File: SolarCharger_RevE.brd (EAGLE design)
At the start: 85 x 78 mm, 134 parts, among them CON1 CON_4X200MIL, CON2 USB_BMULTICOMP, CON3 ICSP, CON4 CON_3X100MIL, CON5 CON_3X100MIL, CON6 CON_8X200MIL, CON7 CON_2X100MIL, CON8 CON_3X100MIL, CON9 CON_6X3X2, IC1 MCP3428, IC10 AT45DB161E, IC11 TPS54428, IC12 MCP14A0153, IC13 MCP14A0153, IC2 INA213, IC3 MIC4605-1YM, IC4 INA213, IC5 PIC18F46J50, IC6 TS6001, IC7 LMT86, IC8 24AA16, IC9 TPS62120, Q1 NX3008NBKW, Q10 NTR4101PT1G, Q11 N-FET, Q12 N-FET, Q13 N-FET, Q14 N-FET, Q15 NX3008NBKW, Q2 PSMN6R0-30YL, Q3 NX3008NBKW, Q4 NTR4101PT1G, Q5 PSMN6R0-30YL, Q6 PSMN6R0-30YL, Q7 NX3008NBKW, Q8 NX3008NBKW, Q9 NX3008NBKW, X1 ABS07-120-32.768KHZ-T, X2 ABM3-8.000MHZ-D2Y-T, X3 USB_A, X4 USB_A

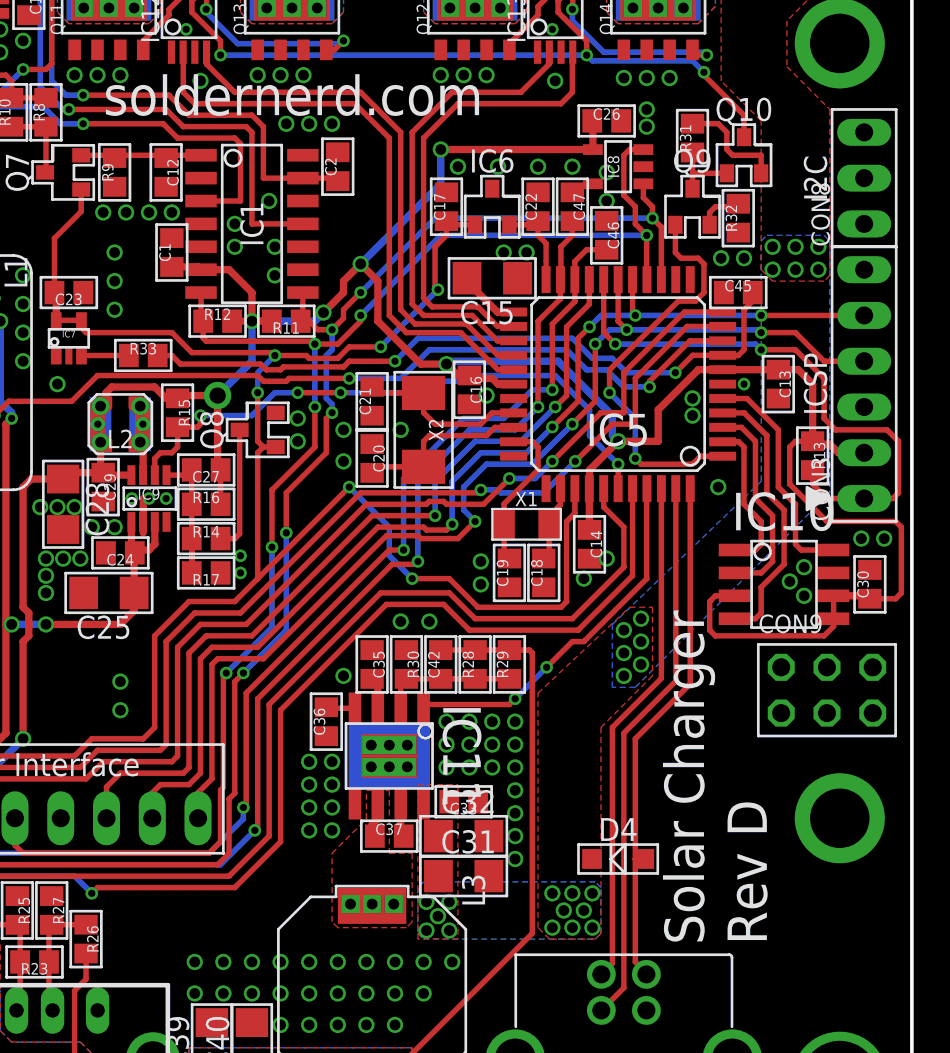
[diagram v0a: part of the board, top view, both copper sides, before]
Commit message: Revision E completed. Now with SPI and I2C headers
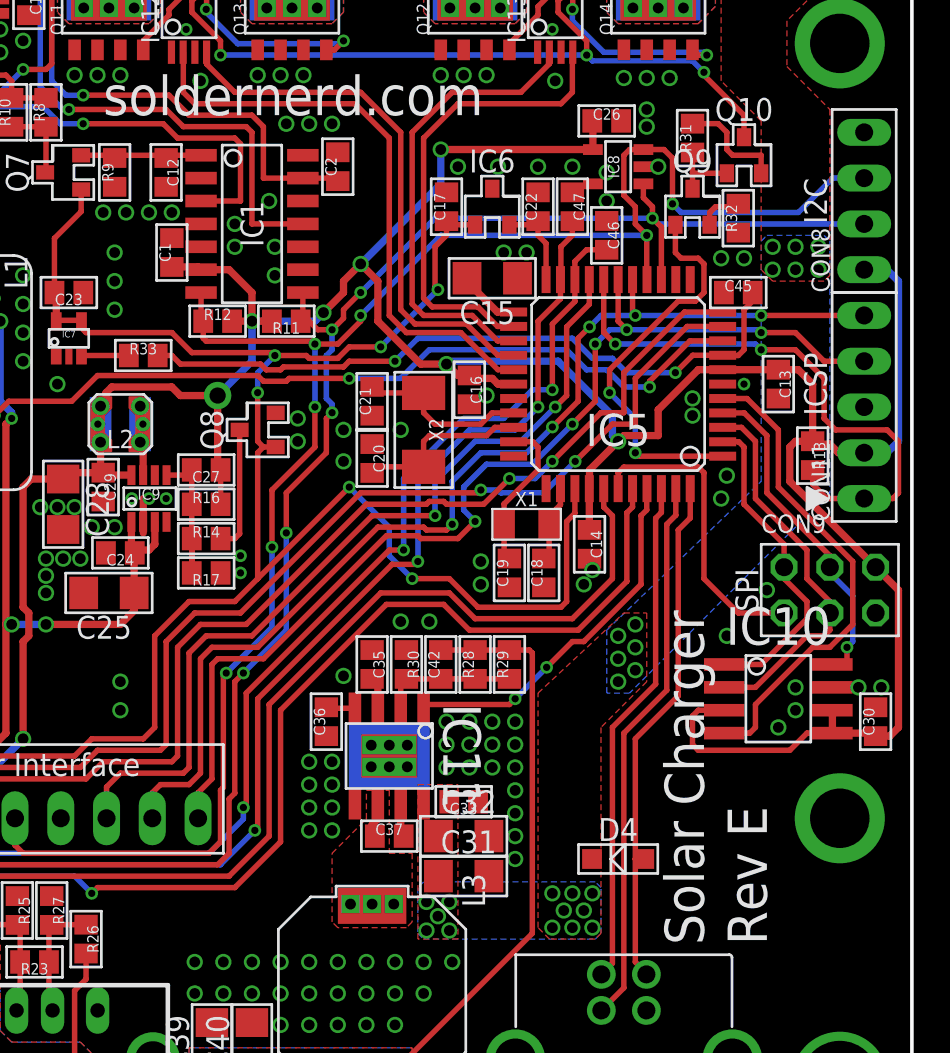
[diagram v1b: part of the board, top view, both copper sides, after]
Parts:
- removed CON3: ICSP, 00Connector:100MIL_6X
- removed R15: 100k, 00Resistor:R0805
- added CON11: CON_5X100MIL, 00Connector:100MIL_5X
- CON8: value CON_3X100MIL -> I2C; device 00Connector:100MIL_3X -> 00Connector:100MIL_4X
- CON9: value CON_6X3X2 -> SPI
- IC10: value AT45DB161E -> AT45DB321E; device 00Logic:SOIC8 -> 00Logic:EIAJ_SOIC8
- moved C30 7.63 mm to (90.5, 22.9)
- moved IC10 6.36 mm to (85.1, 24.1)
- moved CON9 5.56 mm to (87.9, 30.2)
- moved CON8 1.27 mm to (89.9, 51.8)
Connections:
- removed net PWR_GOOD: IC5.39, IC9.6, R15.2
- net !MCLR!: now also CON11.1; no longer CON3.1
- net !SS1!: now also IC5.5; no longer IC5.4
- net !SS2!: now also IC5.39
- net GND: now also CON11.3, CON8.4; no longer CON3.3, CON8.3
- net MISO: now also IC5.4; no longer IC5.5
- net MOSI: now also CON9.1; no longer CON9.3
- net PGC/ENC_A: now also CON11.5; no longer CON3.5
- net PGD/ENC_B: now also CON11.4; no longer CON3.4
- net SCLK: now also CON9.5; no longer CON9.1
- net SDA: now also CON8.3; no longer CON8.1
- net VCC: now also CON11.2, CON8.1, CON9.3; no longer CON3.2, CON9.5, R15.1
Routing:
- net PWR_GOOD: track 34.0 -> 0.00 mm, vias 4 -> 0
- net VCC: track 164.7 -> 183.8 mm
- net !SS2!: track 0.00 -> 17.0 mm
- net SDA: track 81.8 -> 97.8 mm, vias 6 -> 7
- net SCL: track 78.7 -> 90.5 mm
- net !SS1!: track 15.4 -> 26.7 mm
- net SCLK: track 11.6 -> 21.5 mm
- net MOSI: track 8.71 -> 17.9 mm
- net MISO: track 12.8 -> 18.6 mm, vias 0 -> 1
- net OUT_ON: track 22.7 -> 22.1 mm
- net !DISP_EN!: track 61.6 -> 61.0 mm
- net GND: vias 216 -> 220
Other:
- board text added: "A"
- board text added: "B"
- board text added: "January 2018 - Rev E"
- board text added: "MISO"
- board text added: "MOSI"
- board text added: "PB"
- board text added: "PGC"
- board text added: "PGD"
- board text added: "Rev E"
- board text added: "SCL"
- board text added: "SCLK"
- board text added: "SDA"
- board text added: "SPI"
- board text added: "VCC"
- board text added: "~EN"
- board text added: "~MC"
- board text added: "~SS2"
- board text removed: "Rev D"
- board text removed: "September 2017 - Rev D"

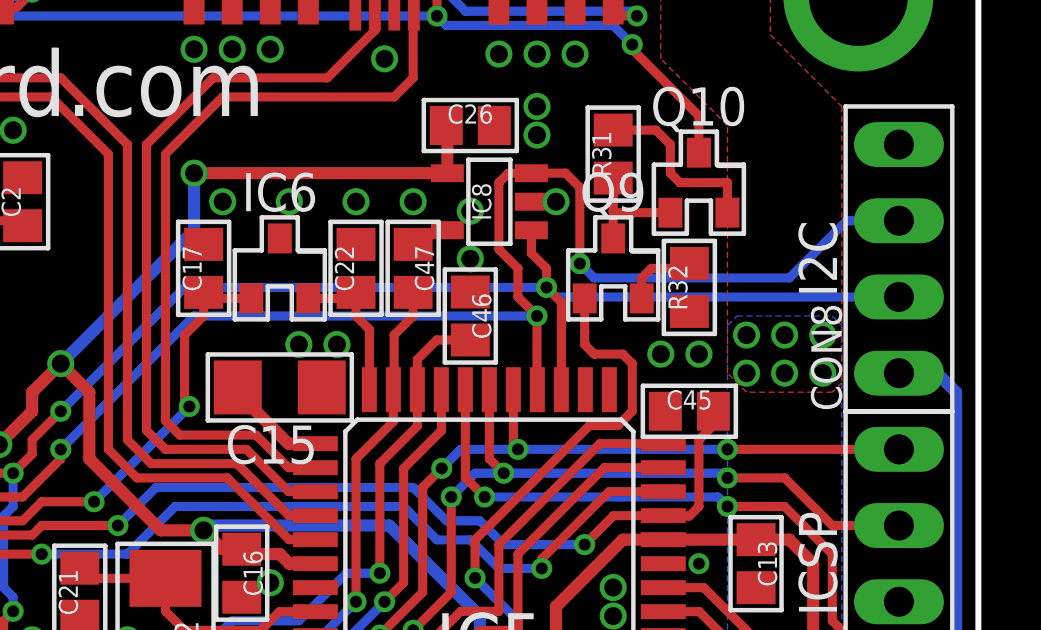
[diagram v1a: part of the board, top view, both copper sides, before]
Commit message: Some ground connections improved
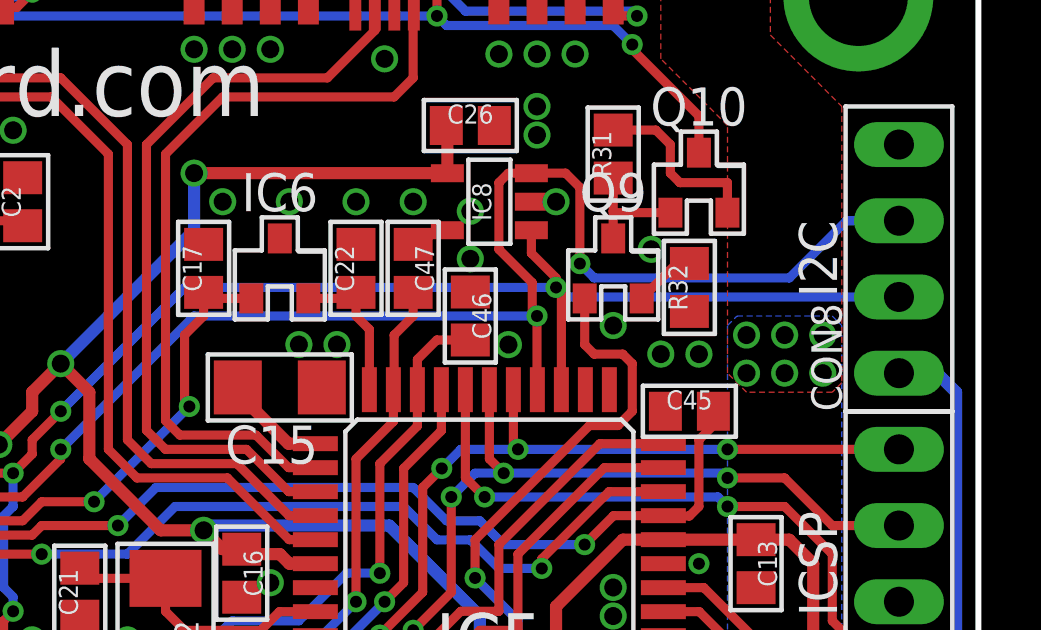
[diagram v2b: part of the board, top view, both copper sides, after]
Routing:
- net GND: vias 220 -> 223
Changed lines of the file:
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@@
 <grid distance="12.5" unitdist="mil" unit="mil" style="lines" multiple="1" display="yes" altdistance="0.025" altunitdist="inch" altunit="inch"/>
 <layers>
-<layer number="1" name="Top" color="4" fill="1" visible="yes" active="yes"/>
+<layer number="1" name="Top" color="4" fill="1" visible="no" active="yes"/>
 <layer number="2" name="Route2" color="1" fill="3" visible="no" active="no"/>
 <layer number="3" name="Route3" color="4" fill="3" visible="no" active="no"/>
@@
 <layer number="17" name="Pads" color="2" fill="1" visible="yes" active="yes"/>
 <layer number="18" name="Vias" color="2" fill="1" visible="yes" active="yes"/>
-<layer number="19" name="Unrouted" color="6" fill="1" visible="yes" active="yes"/>
-<layer number="20" name="Dimension" color="15" fill="1" visible="yes" active="yes"/>
-<layer number="21" name="tPlace" color="7" fill="1" visible="yes" active="yes"/>
-<layer number="22" name="bPlace" color="7" fill="1" visible="yes" active="yes"/>
-<layer number="23" name="tOrigins" color="15" fill="1" visible="yes" active="yes"/>
-<layer number="24" name="bOrigins" color="15" fill="1" visible="yes" active="yes"/>
+<layer number="19" name="Unrouted" color="6" fill="1" visible="no" active="yes"/>
+<layer number="20" name="Dimension" color="15" fill="1" visible="no" active="yes"/>
+<layer number="21" name="tPlace" color="7" fill="1" visible="no" active="yes"/>
+<layer number="22" name="bPlace" color="7" fill="1" visible="no" active="yes"/>
+<layer number="23" name="tOrigins" color="15" fill="1" visible="no" active="yes"/>
+<layer number="24" name="bOrigins" color="15" fill="1" visible="no" active="yes"/>
 <layer number="25" name="tNames" color="7" fill="1" visible="no" active="yes"/>
 <layer number="26" name="bNames" color="7" fill="1" visible="no" active="yes"/>
-<layer number="27" name="tValues" color="7" fill="1" visible="yes" active="yes"/>
-<layer number="28" name="bValues" color="7" fill="1" visible="yes" active="yes"/>
+<layer number="27" name="tValues" color="7" fill="1" visible="no" active="yes"/>
+<layer number="28" name="bValues" color="7" fill="1" visible="no" active="yes"/>
 <layer number="29" name="tStop" color="7" fill="3" visible="no" active="yes"/>
 <layer number="30" name="bStop" color="7" fill="6" visible="no" active="yes"/>
@@
 <text x="87.63" y="37.7825" size="1.27" layer="22" font="vector" ratio="13" rot="MR0" align="center-left">VCC</text>
 <text x="87.63" y="35.2425" size="1.27" layer="22" font="vector" ratio="13" rot="MR0" align="center-left">~MC</text>
-<text x="82.55" y="53.0225" size="1.27" layer="22" font="vector" ratio="13" rot="MR270" align="center">I2C</text>
+<text x="82.55" y="51.7525" size="1.27" layer="22" font="vector" ratio="13" rot="MR270" align="center">I2C</text>
 <text x="82.55" y="41.5925" size="1.27" layer="22" font="vector" ratio="13" rot="MR270" align="center">ICSP</text>
 <wire x1="87.9475" y1="56.8325" x2="87.9475" y2="54.2925" width="0.15" layer="22"/>
@@
 <contactref element="CON11" pad="3"/>
 <contactref element="CON8" pad="4"/>
+<via x="76.835" y="48.895" extent="1-16" drill="0.6"/>
+<via x="81.5975" y="52.07" extent="1-16" drill="0.6"/>
+<via x="80.3275" y="49.53" extent="1-16" drill="0.6"/>
 </signal>
 <signal name="VIN" class="1">
@@
 <contactref element="R32" pad="2"/>
 <contactref element="Q9" pad="2"/>
-<wire x1="81.2775" y1="50.435" x2="81.2775" y2="51.115" width="0.3048" layer="1"/>
-<wire x1="81.2775" y1="51.115" x2="81.5975" y2="51.435" width="0.3048" layer="1"/>
-<wire x1="81.5975" y1="51.435" x2="82.7025" y2="51.435" width="0.3048" layer="1"/>
 <wire x1="82.7025" y1="51.435" x2="82.8675" y2="51.6" width="0.3048" layer="1"/>
+<wire x1="82.8675" y1="51.6" x2="82.4425" y2="51.6" width="0.3048" layer="1"/>
+<wire x1="82.4425" y1="51.6" x2="81.2775" y2="50.435" width="0.3048" layer="1"/>
 </signal>
 <signal name="N$36">
@@
 <via x="61.9125" y="46.6725" extent="1-16" drill="0.4"/>
 <wire x1="61.9125" y1="46.6725" x2="66.04" y2="50.8" width="0.3048" layer="16"/>
-<wire x1="66.04" y1="50.8" x2="78.105" y2="50.8" width="0.3048" layer="16"/>
-<via x="78.105" y="50.8" extent="1-16" drill="0.4"/>
-<wire x1="78.2825" y1="50.6225" x2="78.105" y2="50.8" width="0.3048" layer="1"/>
+<wire x1="66.04" y1="50.8" x2="78.4225" y2="50.8" width="0.3048" layer="16"/>
+<via x="78.4225" y="50.8" extent="1-16" drill="0.4"/>
 <via x="55.40375" y="25.55875" extent="1-16" drill="0.4"/>
 <wire x1="55.40375" y1="25.55875" x2="57.785" y2="27.94" width="0.3048" layer="16"/>
@@
 <wire x1="60.325" y1="43.4975" x2="60.325" y2="44.60875" width="0.3048" layer="16"/>
 <via x="60.325" y="44.60875" extent="1-16" drill="0.4"/>
-<wire x1="78.6" y1="47.3925" x2="78.6" y2="50.305" width="0.3048" layer="1"/>
-<wire x1="78.6" y1="50.305" x2="78.105" y2="50.8" width="0.3048" layer="1"/>
+<wire x1="78.6" y1="47.3925" x2="78.6" y2="50.6225" width="0.3048" layer="1"/>
+<wire x1="78.6" y1="50.6225" x2="78.4225" y2="50.8" width="0.3048" layer="1"/>
 <wire x1="77.6" y1="52.7075" x2="77.6" y2="51.94" width="0.3048" layer="1"/>
-<wire x1="77.6" y1="51.94" x2="78.105" y2="51.435" width="0.3048" layer="1"/>
-<wire x1="78.105" y1="51.435" x2="78.105" y2="50.8" width="0.3048" layer="1"/>
+<wire x1="77.6" y1="51.94" x2="78.4225" y2="51.1175" width="0.3048" layer="1"/>
+<wire x1="78.4225" y1="51.1175" x2="78.4225" y2="50.8" width="0.3048" layer="1"/>
 <wire x1="60.325" y1="44.60875" x2="60.96" y2="45.24375" width="0.3048" layer="1"/>
 <wire x1="60.96" y1="45.24375" x2="60.96" y2="45.72" width="0.3048" layer="1"/>
@@
 <wire x1="40.9575" y1="14.9225" x2="40.19" y2="15.69" width="0.3048" layer="1"/>
 <wire x1="40.19" y1="15.69" x2="40.19" y2="17.5" width="0.3048" layer="1"/>
-<wire x1="89.8525" y1="50.4825" x2="78.4225" y2="50.4825" width="0.3048" layer="16"/>
-<wire x1="78.4225" y1="50.4825" x2="78.105" y2="50.8" width="0.3048" layer="16"/>
+<wire x1="89.8525" y1="50.4825" x2="78.74" y2="50.4825" width="0.3048" layer="16"/>
+<wire x1="78.74" y1="50.4825" x2="78.4225" y2="50.8" width="0.3048" layer="16"/>
 <contactref element="CON8" pad="2"/>
 </signal>
@@
 <wire x1="76.8325" y1="54.6075" x2="76.5175" y2="54.2925" width="0.3048" layer="1"/>
 <wire x1="76.5175" y1="54.2925" x2="76.5175" y2="52.07" width="0.3048" layer="1"/>
-<wire x1="76.5175" y1="52.07" x2="77.1525" y2="51.435" width="0.3048" layer="1"/>
-<wire x1="77.1525" y1="51.435" x2="77.1525" y2="50.4825" width="0.3048" layer="1"/>
-<wire x1="77.1525" y1="50.4825" x2="77.7875" y2="49.8475" width="0.3048" layer="1"/>
+<wire x1="76.5175" y1="52.07" x2="77.62875" y2="50.95875" width="0.3048" layer="1"/>
+<wire x1="77.62875" y1="50.95875" x2="77.62875" y2="50.00625" width="0.3048" layer="1"/>
+<wire x1="77.62875" y1="50.00625" x2="77.7875" y2="49.8475" width="0.3048" layer="1"/>
 <wire x1="53.175" y1="45.085" x2="53.055" y2="45.205" width="0.3048" layer="1"/>
 <wire x1="53.055" y1="45.205" x2="53.055" y2="46.6725" width="0.3048" layer="1"/>
